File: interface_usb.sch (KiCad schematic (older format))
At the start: 5 parts, among them U45 CP2110, U46 ESDR0502N, U47 CONN_USB

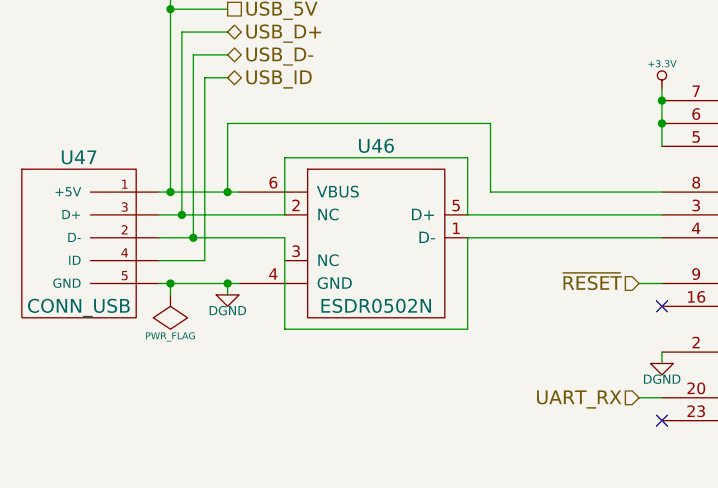
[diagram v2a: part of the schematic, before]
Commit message: routed 70% of board, made adjustments to schematics as necessary
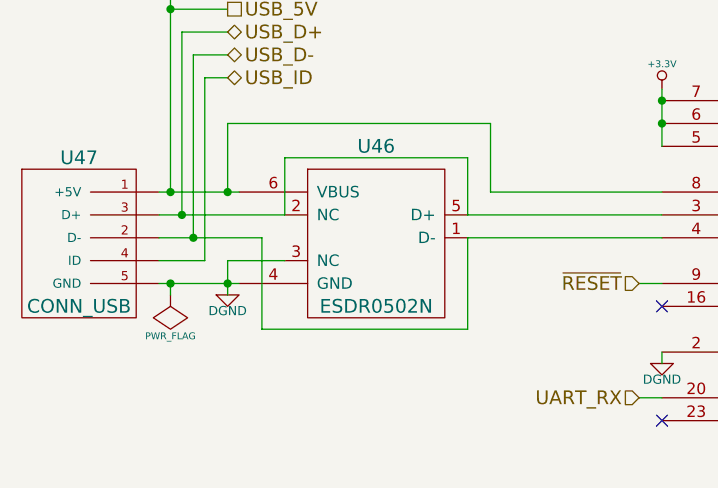
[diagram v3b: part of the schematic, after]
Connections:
- net DGND: now also U46.3 (NC)
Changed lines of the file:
@@
 Sheet 15 16
 Title ""
-Date "10 feb 2014"
+Date "13 feb 2014"
 Rev ""
 Comp ""
@@
 	1750 3050 1750 2800
 Wire Wire Line
-	1750 3150 1750 3550
-Wire Wire Line
 	1200 2950 1550 2950
 Wire Wire Line
 	1200 3350 1550 3350
 Wire Wire Line
-	1500 3350 1500 3400
+	1500 3250 1500 3400
 Connection ~ 1500 3350
 Wire Wire Line
@@
 Wire Wire Line
 	1200 3050 1750 3050
-Wire Wire Line
-	1200 3150 1750 3150
 Wire Wire Line
 	3400 2500 3400 2750
@@
 	2550 3050 2550 2800
 Wire Wire Line
-	2550 3150 2550 3550
-Wire Wire Line
-	2550 3550 1750 3550
-Wire Wire Line
 	2550 2800 1750 2800
 Text HLabel 4050 2000 0    60   Input ~ 0
@@
 	1250 3400 1250 3350
 Connection ~ 1250 3350
+Wire Wire Line
+	1750 3250 1500 3250
+Wire Wire Line
+	1200 3150 1650 3150
+Wire Wire Line
+	1650 3150 1650 3550
+Wire Wire Line
+	1650 3550 2550 3550
+Wire Wire Line
+	2550 3550 2550 3150
 $EndSCHEMATC

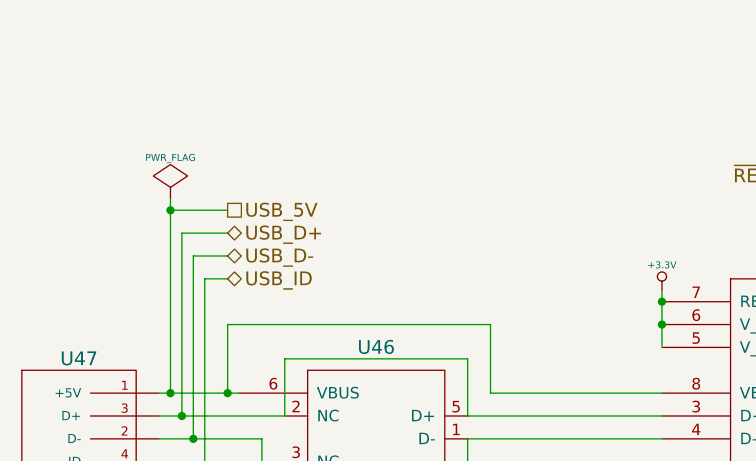
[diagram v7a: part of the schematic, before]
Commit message: added connector for testing solar panel
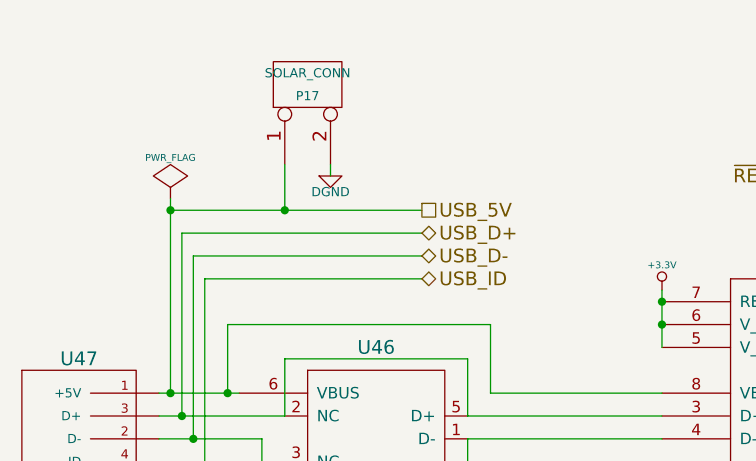
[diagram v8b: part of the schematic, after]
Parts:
- added P17: SOLAR_CONN, symbol CONN_2
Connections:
- net DGND: now also P17.2 (PM)
- net USB_5V: now also P17.1 (P1)
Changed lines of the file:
@@
 $Descr A4 11693 8268
 encoding utf-8
-Sheet 15 16
+Sheet 14 16
 Title ""
-Date "27 feb 2014"
+Date "1 mar 2014"
 Rev ""
 Comp ""
@@
 	1250 2100 1250 2950
 Wire Wire Line
-	1250 2150 1500 2150
+	1250 2150 2350 2150
 Connection ~ 1250 2950
 Wire Wire Line
 	1300 3050 1300 2250
 Wire Wire Line
-	1300 2250 1500 2250
+	1300 2250 2350 2250
 Connection ~ 1300 3050
 Wire Wire Line
 	1350 3150 1350 2350
 Wire Wire Line
-	1350 2350 1500 2350
+	1350 2350 2350 2350
 Connection ~ 1350 3150
 Wire Wire Line
@@
 	1400 3250 1400 2450
 Wire Wire Line
-	1400 2450 1500 2450
-Text HLabel 1500 2150 2    60   UnSpc ~ 0
+	1400 2450 2350 2450
+Text HLabel 2350 2150 2    60   UnSpc ~ 0
 USB_5V
-Text HLabel 1500 2250 2    60   BiDi ~ 0
+Text HLabel 2350 2250 2    60   BiDi ~ 0
 USB_D+
-Text HLabel 1500 2350 2    60   BiDi ~ 0
+Text HLabel 2350 2350 2    60   BiDi ~ 0
 USB_D-
-Text HLabel 1500 2450 2    60   BiDi ~ 0
+Text HLabel 2350 2450 2    60   BiDi ~ 0
 USB_ID
 Wire Wire Line
@@
 Wire Wire Line
 	2550 3550 2550 3150
+$Comp
+L CONN_2 P17
+U 1 1 5311308F
+P 1850 1600
+F 0 "P17" V 1800 1600 40  0000 C CNN
+F 1 "SOLAR_CONN" V 1900 1600 40  0000 C CNN
+F 2 "" H 1850 1600 60  0000 C CNN
+F 3 "" H 1850 1600 60  0000 C CNN
+	1    1850 1600
+	0    -1   -1   0
+$EndComp
+Wire Wire Line
+	1750 1950 1750 2150
+Connection ~ 1750 2150
+$Comp
+L DGND #PWR098
+U 1 1 531130EB
+P 1950 2000
+F 0 "#PWR098" H 1950 2000 40  0001 C CNN
+F 1 "DGND" H 1950 1930 40  0000 C CNN
+F 2 "" H 1950 2000 60  0000 C CNN
+F 3 "" H 1950 2000 60  0000 C CNN
+	1    1950 2000
+	1    0    0    -1
+$EndComp
+Wire Wire Line
+	1950 1950 1950 2000
 $EndSCHEMATC
